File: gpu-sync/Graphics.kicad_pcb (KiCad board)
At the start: 2 copper layers, 160 x 100 mm, 68 parts, among them J1 C96ABC, J2 Conn_01x26_Male, SW1 SW_Coded_SH-7050, U1 74AC161, U10 74HC688, U11 74HC688, U12 74HC688, U13 74HC688, U14 74HC688, U15 74HC04, U16 74HC109, U17 74HC109, U18 74AC573, U19 74AC573, U2 74AC161, U20 74AC573, U21 74AC573, U22 74AC573, U23 74AC573, U24 74AC573, U25 74AC573, U26 74AC573, U27 74AC573, U28 74AC573, U29 74HC688, U3 74AC161, U30 74AC138, U31 74AC138, U32 74HC00, U33 74HC00, U34 74HC00, U4 74AC161, U5 74AC161, U6 74AC161, U7 74HC688, U8 74HC688, U9 74HC688, X1 25.175MHz

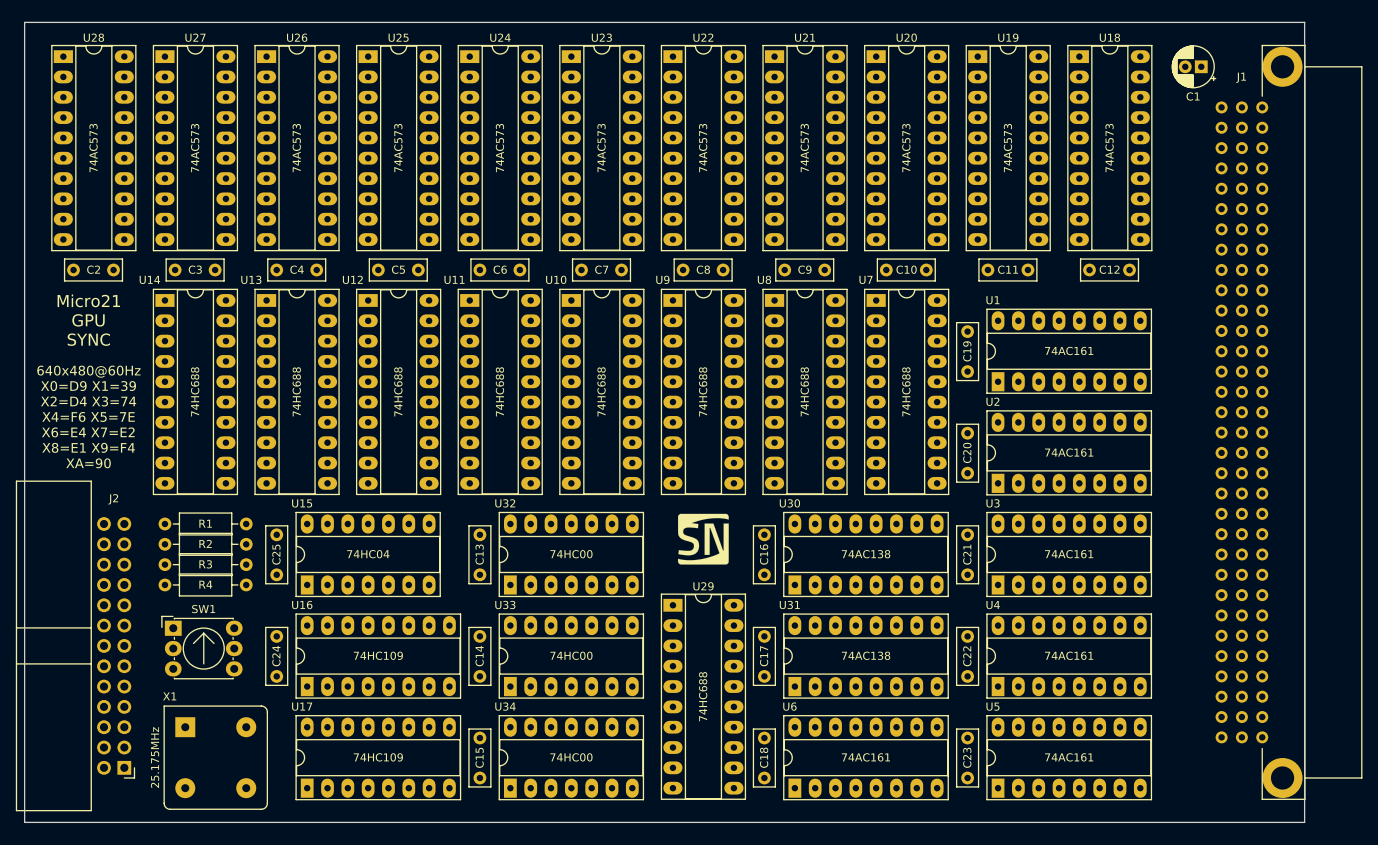
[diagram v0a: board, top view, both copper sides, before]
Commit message: gpu sync board routed
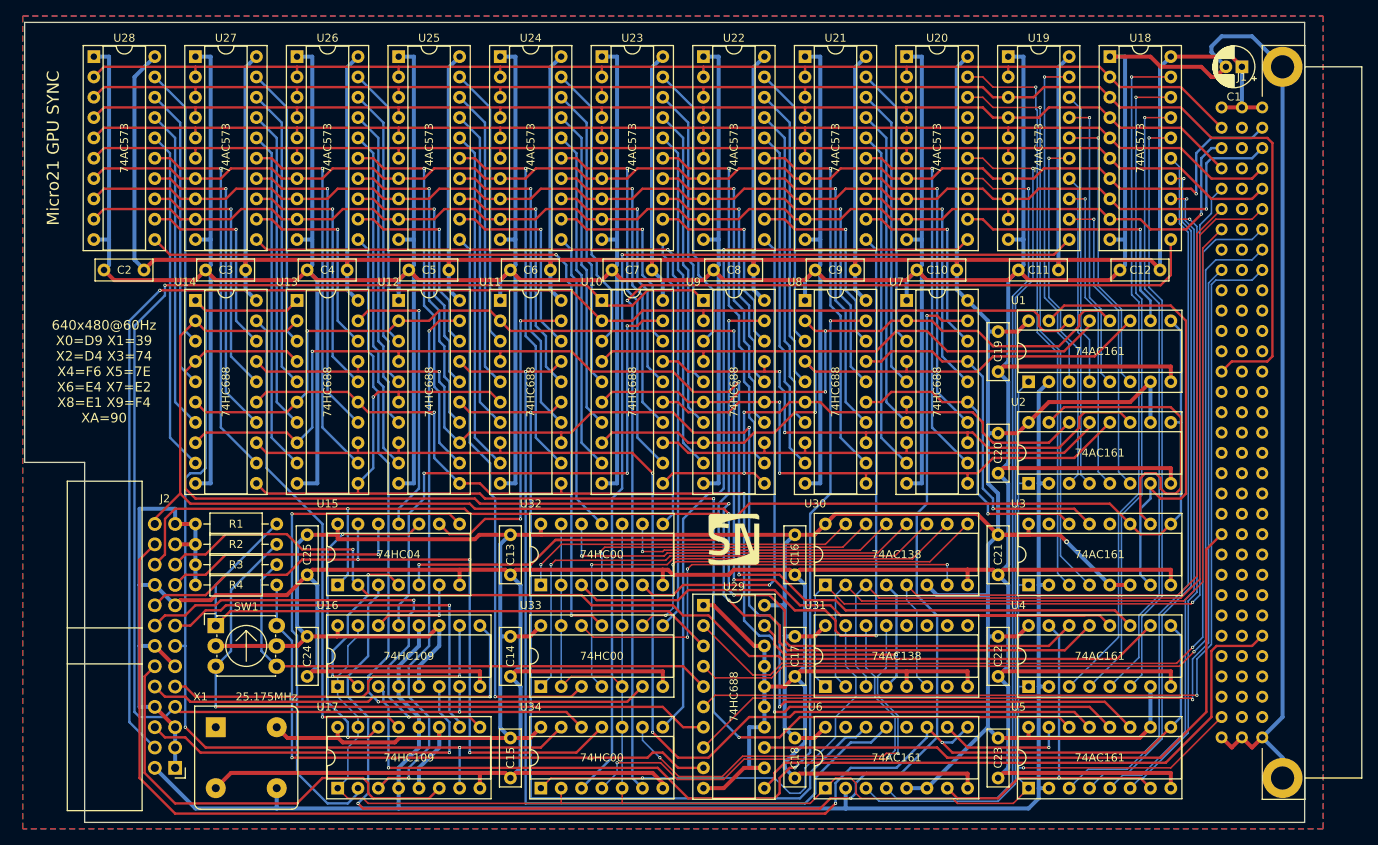
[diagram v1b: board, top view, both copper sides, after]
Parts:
- U1, U16, U17, U2, U3, U30, U31, U4, U5, U6: footprint Package_DIP:DIP-16_W7.62mm_Socket_LongPads -> Package_DIP:DIP-16_W7.62mm_Socket
- U10, U11, U12, U13, U14, U18, U19, U20, U21, U22, U23, U24, U25, U26, U27, U28, U29, U7, U8, U9: footprint Package_DIP:DIP-20_W7.62mm_Socket_LongPads -> Package_DIP:DIP-20_W7.62mm_Socket
- U15, U32, U33, U34: footprint Package_DIP:DIP-14_W7.62mm_Socket_LongPads -> Package_DIP:DIP-14_W7.62mm_Socket
- moved R1 14.0 mm to (81.5, 112.7), turned to 180 degrees
- moved R2 14.0 mm to (81.5, 115.2), turned to 180 degrees
- moved R3 14.0 mm to (81.5, 117.8), turned to 180 degrees
- moved R4 14.0 mm to (81.5, 120.3), turned to 180 degrees
- moved J2 6.35 mm to (68.8, 143.2)
- moved SW1 5.32 mm to (73.9, 125.4)
- moved C1 5.08 mm to (202.2, 55.5)
- moved C10 3.81 mm to (161.5, 81.0)
- moved C11 3.81 mm to (174.2, 81.0)
- moved C13 3.81 mm to (110.7, 119.0)
- moved C14 3.81 mm to (110.7, 131.8)
- moved C15 3.81 mm to (110.7, 144.4)
- moved C16 3.81 mm to (146.3, 119.0)
- moved C17 3.81 mm to (146.3, 131.8)
- moved C18 3.81 mm to (146.3, 144.4)
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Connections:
- SW1 pad 2: Net-(R2-Pad1) -> Net-(R3-Pad1)
- SW1 pad 4: Net-(R3-Pad1) -> Net-(R2-Pad1)
- U15 pad 14: (no net) -> VCC
- U15 pad 7: (no net) -> GND
- U16 pad 16: (no net) -> VCC
- U16 pad 8: (no net) -> GND
- U17 pad 16: (no net) -> VCC
- U17 pad 8: (no net) -> GND
- U18 pad 12: /Column Counter/D7 -> /Row Counter/D7
- U18 pad 13: /Column Counter/D6 -> /Row Counter/D6
- U18 pad 14: /Column Counter/D5 -> /Row Counter/D5
- U18 pad 15: /Column Counter/D4 -> /Row Counter/D4
- U18 pad 16: /Column Counter/D3 -> /Row Counter/D3
- U18 pad 17: /Column Counter/D2 -> /Row Counter/D2
- U18 pad 18: /Column Counter/D1 -> /Row Counter/D1
- U18 pad 19: /Column Counter/D0 -> /Row Counter/D0
- U19 pad 12: /Row Counter/D7 -> /Column Counter/D7
- U19 pad 13: /Row Counter/D6 -> /Column Counter/D6
- U19 pad 14: /Row Counter/D5 -> /Column Counter/D5
- U19 pad 15: /Row Counter/D4 -> /Column Counter/D4
- U19 pad 16: /Row Counter/D3 -> /Column Counter/D3
- U19 pad 17: /Row Counter/D2 -> /Column Counter/D2
- U19 pad 18: /Row Counter/D1 -> /Column Counter/D1
- U19 pad 19: /Row Counter/D0 -> /Column Counter/D0
- U29 pad 5: Net-(R2-Pad1) -> Net-(R3-Pad1)
- U29 pad 7: Net-(R3-Pad1) -> Net-(R2-Pad1)
- U32 pad 14: (no net) -> VCC
- U32 pad 7: (no net) -> GND
- U33 pad 14: (no net) -> VCC
- U33 pad 7: (no net) -> GND
- U34 pad 14: (no net) -> VCC
- U34 pad 3: Net-(U18-Pad11) -> Net-(U19-Pad11)
- U34 pad 6: Net-(U19-Pad11) -> Net-(U18-Pad11)
- U34 pad 7: (no net) -> GND
- X1 pad 1: /Column Counter/CE -> Net-(X1-Pad1)
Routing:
- net GND: track 0.00 -> 1484.6 mm
- net VCC: track 0.00 -> 925.6 mm, vias 0 -> 1
- net ~RESET: track 0.00 -> 264.9 mm, vias 0 -> 1
- net /PCLK: track 0.00 -> 202.5 mm
- net D1: track 0.00 -> 195.8 mm
- net /~TCR: track 0.00 -> 187.8 mm, vias 0 -> 2
- net /~HBLANK: track 0.00 -> 185.5 mm, vias 0 -> 2
- net /VBLANK Generator/P0: track 0.00 -> 182.6 mm, vias 0 -> 3
- net /HSYNC Generator/P0: track 0.00 -> 179.4 mm, vias 0 -> 1
- net /~TCC: track 0.00 -> 173.7 mm, vias 0 -> 1
- net /VSYNC Generator/P0: track 0.00 -> 169.8 mm, vias 0 -> 2
- net Net-(U15-Pad3): track 0.00 -> 167.2 mm, vias 0 -> 3
- net D5: track 0.00 -> 163.8 mm, vias 0 -> 1
- net D6: track 0.00 -> 163.6 mm, vias 0 -> 1
- net /VBLANK Generator/P2: track 0.00 -> 162.7 mm, vias 0 -> 3
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- added copper zone on B.Cu, net GND
- added copper zone on F.Cu, net GND
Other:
- outline, holes or cut-outs redrawn
- net class Default: clearance 0.2 -> 0.175; trace_width 0.25 -> 0.3; via_dia 0.8 -> 0.4; via_drill 0.4 -> 0.2
- net class Fine added: clearance 0.15, trace_width 0.2, via_dia 0.4, via_drill 0.2
- net class POWER added: clearance 0.175, trace_width 0.5, via_dia 0.6, via_drill 0.3
- rule trace_clearance: 0.2 -> 0.175
- rule trace_min: 0.2 -> 0.125
- rule via_min_drill: 0.3 -> 0.2
- rule via_min_size: 0.4 -> 0.325

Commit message: leave space for guide rails
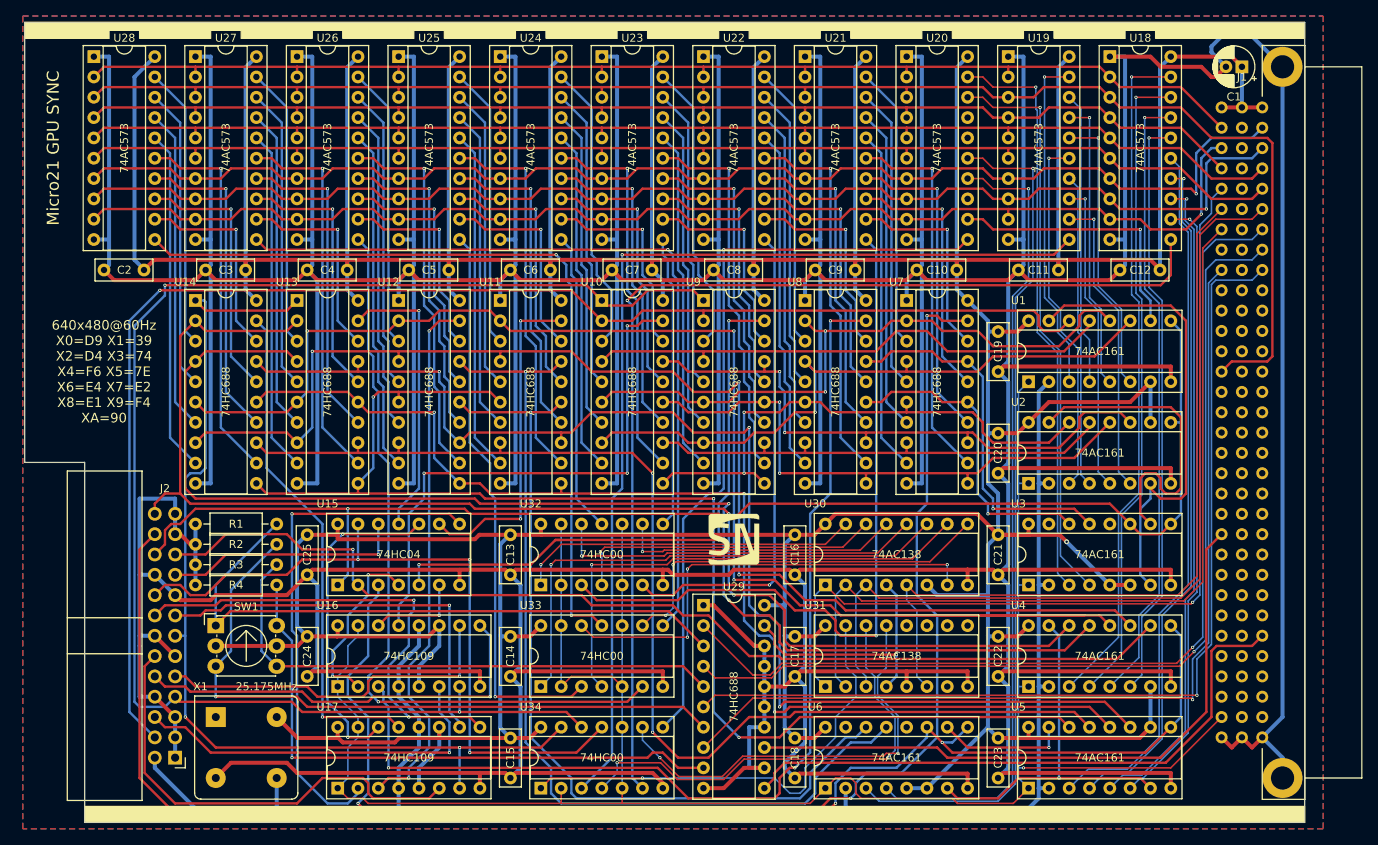
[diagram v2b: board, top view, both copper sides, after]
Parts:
- moved J2 1.27 mm to (68.8, 141.9)
- moved X1 1.27 mm to (73.9, 136.8)
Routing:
- net /VBLANK Generator/P6: track 108.7 -> 105.4 mm
- net /VBLANK Generator/P7: track 117.9 -> 115.3 mm
- net GND: track 1484.6 -> 1486.9 mm
- net /~TCC: track 173.7 -> 171.6 mm
- net /PCLK: track 202.5 -> 204.4 mm
- net /~TCR: track 187.8 -> 189.1 mm
- net /HSYNC Generator/P0: track 179.4 -> 178.1 mm
- net /VBLANK: track 55.9 -> 57.2 mm
- net /~HBLANK: track 185.5 -> 184.7 mm
- net Net-(R2-Pad1): track 85.5 -> 84.7 mm
- net /BLANK: track 88.1 -> 88.7 mm
- net /~VSYNC: track 60.1 -> 59.6 mm
- net /~HSYNC: track 52.4 -> 52.9 mm
- net /VSYNC: track 51.1 -> 50.6 mm
- net /HSYNC: track 44.2 -> 44.8 mm
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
